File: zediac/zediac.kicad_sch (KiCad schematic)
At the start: 135 parts, among them J1 Conn_02x20_Odd_Even, J2 Conn_01x03_Male, J3 Conn_02x12_Odd_Even, J4 Conn_01x03_Male, J5 Conn_02x05_Odd_Even, J6 Conn_01x03_Male, J7 Screw_Terminal_01x02, J8 Barrel_Jack, P1 USB_C_Plug_USB2.0, Q1 Q_PMOS_GDS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

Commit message: Add silk labels for connectors and jumpers
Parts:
- G1: footprint (none) -> zediac:zediac-logo
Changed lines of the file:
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@@
       (effects (font (size 1.27 1.27)) hide)
     )
-    (property "Footprint" "" (id 2) (at 496.57 363.855 0)
+    (property "Footprint" "zediac:zediac-logo" (id 2) (at 496.57 363.855 0)
       (effects (font (size 1.27 1.27)) hide)
     )
@@
     )
     (path "/c6ab306e-e6a9-4bf2-b543-654c4f8e78f7"
-      (reference "G1") (unit 1) (value "LOGO") (footprint "")
+      (reference "G1") (unit 1) (value "LOGO") (footprint "zediac:zediac-logo")
     )
     (path "/cea4748c-6d2d-4633-98b5-6fee26e30e0f"

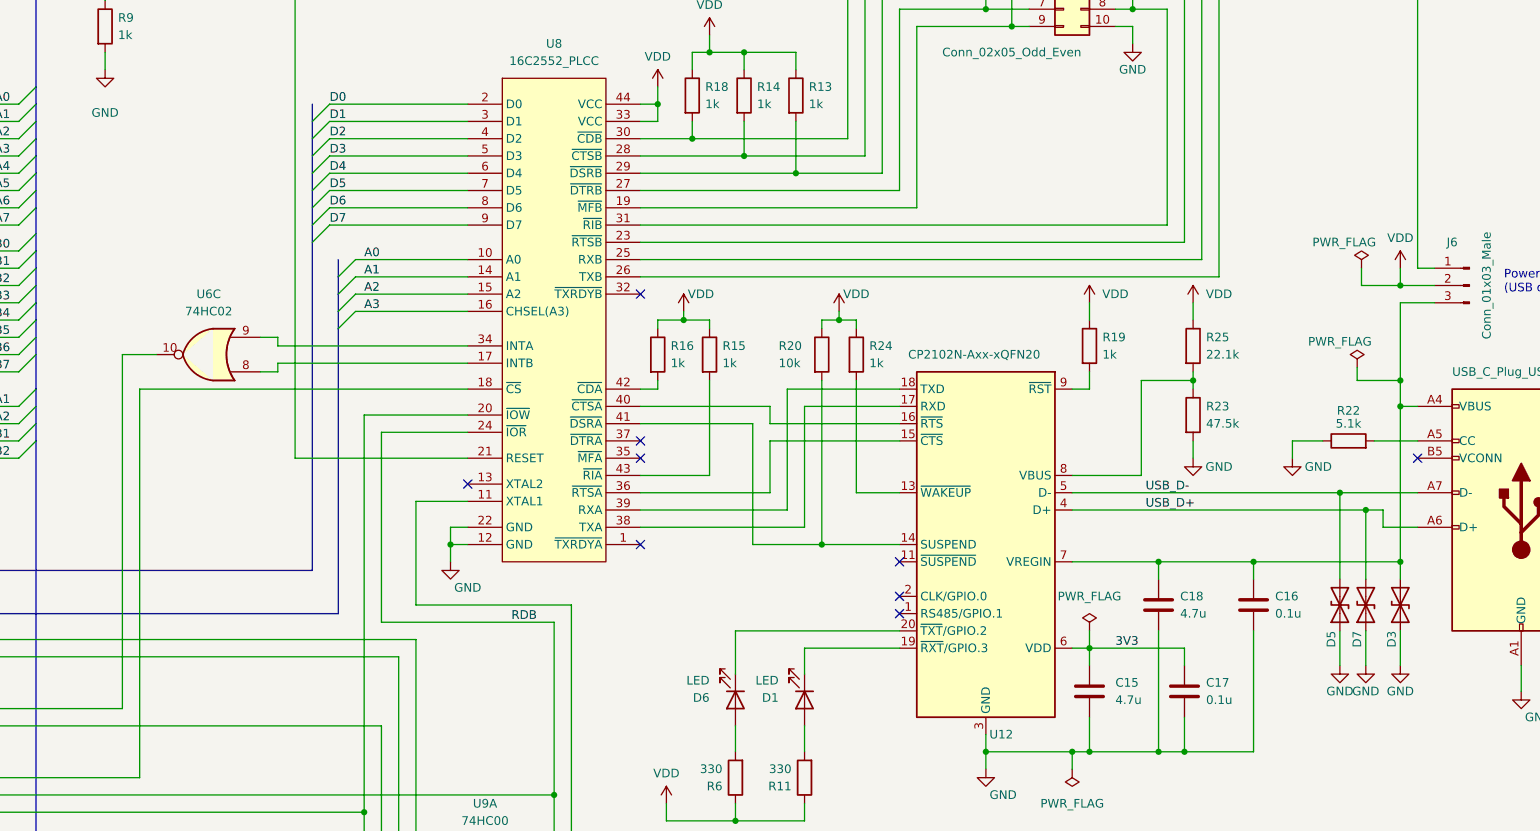
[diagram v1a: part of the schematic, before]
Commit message: Silk cleanup; add UART INT pulldown resistors
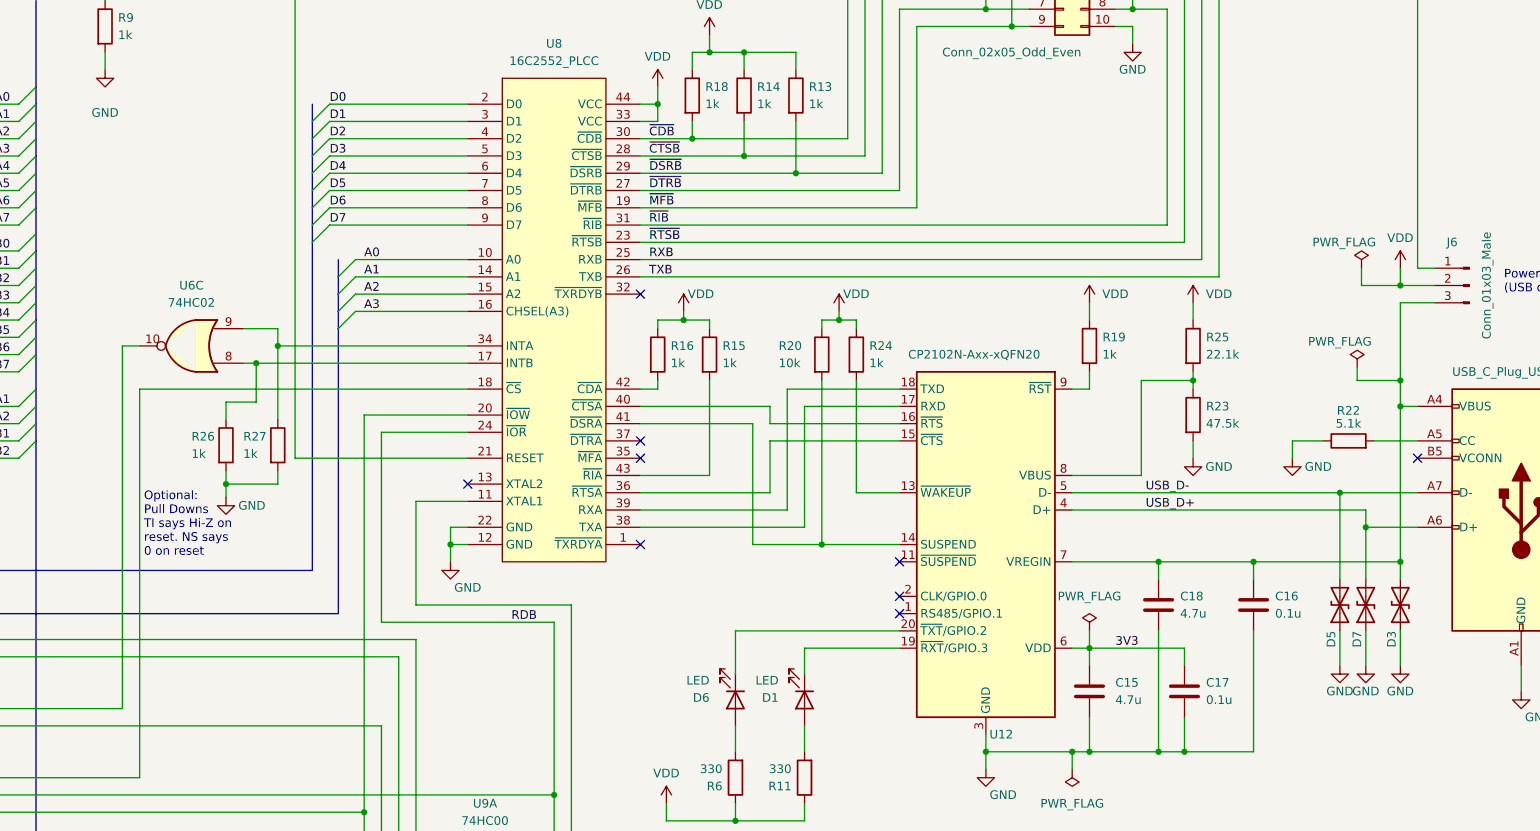
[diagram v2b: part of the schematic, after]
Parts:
- added R26, R27: 1k, Resistor_THT:R_Axial_DIN0207_L6.3mm_D2.5mm_P7.62mm_Horizontal, symbol Device:R
- TP1, TP2: footprint TestPoint:TestPoint_Bridge_Pitch2.54mm_Drill1.0mm -> TestPoint:TestPoint_Keystone_5000-5004_Miniature
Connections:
- net GND: now also R26.2, R27.2
- net ~{RIB}: now reaches D16.1 (A1), J5.8 (Pin_8), U8.31 (~{RIB})
- net ~{CDB}: now reaches D12.1 (A1), J5.1 (Pin_1), R18.2, U8.30 (~{CDB})
- net ~{CTSB}: now reaches D11.1 (A1), J5.3 (Pin_3), R14.2, U8.28 (~{CTSB})
- net ~{DTRB}: now reaches D9.1 (A1), J5.7 (Pin_7), U8.27 (~{DTRB})
- net at U6.8, U8.17 (INTB): now also R26.1
- net ~{MFB}: now reaches D8.1 (A1), J5.9 (Pin_9), U8.19 (~{MFB})
- net ~{RTSB}: now reaches D13.1 (A1), J5.6 (Pin_6), U8.23 (~{RTSB})
- net RXB: now reaches D15.1 (A1), J5.4 (Pin_4), U8.25 (RXB)
- net TXB: now reaches D14.1 (A1), J5.2 (Pin_2), U8.26 (TXB)
- net ~{DSRB}: now reaches D10.1 (A1), J5.5 (Pin_5), R13.2, U8.29 (~{DSRB})
- net at U6.9, U8.34 (INTA): now also R27.1
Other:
- note added: "Optional: Pull Downs TI says Hi-Z on reset. NS says 0 on reset"
- moved on the sheet: U6C
